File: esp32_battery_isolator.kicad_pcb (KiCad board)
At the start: 4 copper layers, 67.8 x 65.8 mm, 88 parts, among them J1 BATT1, J2 Conn_01x04_Female, J3 USB_B_Micro, J4 BATT2, J5 LOAD1, J6 CHGR, J7 LOAD2, J8 LOAD3, J9 Conn_01x03_Male, Q1 MMBT3904, Q10 AONR21321, Q11 AONR21321, Q12 MMBT3904, Q13 AONR21321, Q2 AONR21321, Q3 MMBT3904, Q4 AONR21321, Q5 MMBT3904, Q6 AONR21321, Q7 MMBT3904, Q8 AONR21321, Q9 MMBT3904, SW1 C492887, SW2 C492887, U1 ESP32-WROOM-32D, U2 XL1509_SOP8, U3 ADC128D818, U4 CC6903SO-30A, U5 CH340N, U6 CC6903SO-30A

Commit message: closer
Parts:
- removed Q13, Q6: AONR21321, Acea:DFN-TRANS_AONR21321
- removed Q5: MMBT3904, Package_TO_SOT_SMD:SOT-23
- removed R15: 200k, Resistor_SMD:R_0603_1608Metric
- removed R25: 11k, Resistor_SMD:R_0603_1608Metric
- removed R29: 510R, Resistor_SMD:R_0603_1608Metric
- added BZ1: Buzzer, Buzzer_Beeper:SMDBuzzer_C201046, F.Cu at (171.9, 122.0)
- Q10, Q11, Q2, Q4, Q8: value AONR21321 -> AONR21357
- moved U4 2.90 mm to (128.1, 96.8)
- moved U6 2.25 mm to (123.9, 104.7)
- moved Q4 1.38 mm to (122.2, 88.0)
- moved Ref** 1.34 mm to (111.5, 122.8)
- moved J2 1.13 mm to (158.0, 90.6)
- moved Q11 0.92 mm to (122.2, 92.2)
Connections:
- J9 pad 1: B2C -> COM
- Q10 pad S: B2C -> COM
- Q2 pad S: B2C -> COM
- Q8 pad S: B2C -> COM
- R14 pad 1: B1VM -> COM
- R16 pad 1: B2VM -> COM
- R17 pad 1: B2VM -> COM
- R20 pad 1: B2VM -> COM
- U1 pad 10: B2ON -> (no net)
- U1 pad 30: (no net) -> BZR
- U5 pad 4: (no net) -> RST
- U6 pad 3: B2C -> COM
- U6 pad 4: B2C -> COM
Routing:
- net BZR: track 0.00 -> 52.8 mm, vias 0 -> 4
- net COM: track 0.00 -> 37.4 mm, vias 3 -> 38
- net RST: track 46.1 -> 74.1 mm, vias 0 -> 2
- net Net-(Q13-PadG): track 22.5 -> 0.00 mm
- net B2VM: track 224.4 -> 209.4 mm, vias 14 -> 12
- net B2ON: track 13.1 -> 0.00 mm
- net Net-(Q5-Pad1): track 3.46 -> 0.00 mm
- net B1CM: track 46.1 -> 49.0 mm
- net L1ON: track 23.4 -> 25.9 mm
- net +3V3: track 138.2 -> 136.5 mm
- net B2C: track 1.60 -> 0.00 mm, vias 66 -> 0
- net Net-(Q1-Pad3): track 13.9 -> 14.9 mm
- net GND: track 72.5 -> 71.6 mm
- net L2ON: track 23.8 -> 24.4 mm
- net SCL: track 31.6 -> 31.1 mm
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- added copper zone on In2.Cu, net COM
- removed copper zone on B.Cu, net B2C
- removed copper zone on F.Cu, net B2C
- removed copper zone on In2.Cu, net B2C
- removed copper zone on B.Cu, net Net-(Q13-PadD)
- removed copper zone on F.Cu, net Net-(Q13-PadD)
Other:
- board text added: "ALARM"
- board text added: "CHGR"
- board text added: "ISOLATOR V1"
- board text removed: "B3/ CHG"

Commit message: closer
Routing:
- net L2ON: track 24.4 -> 26.3 mm
- net COM: vias 38 -> 39

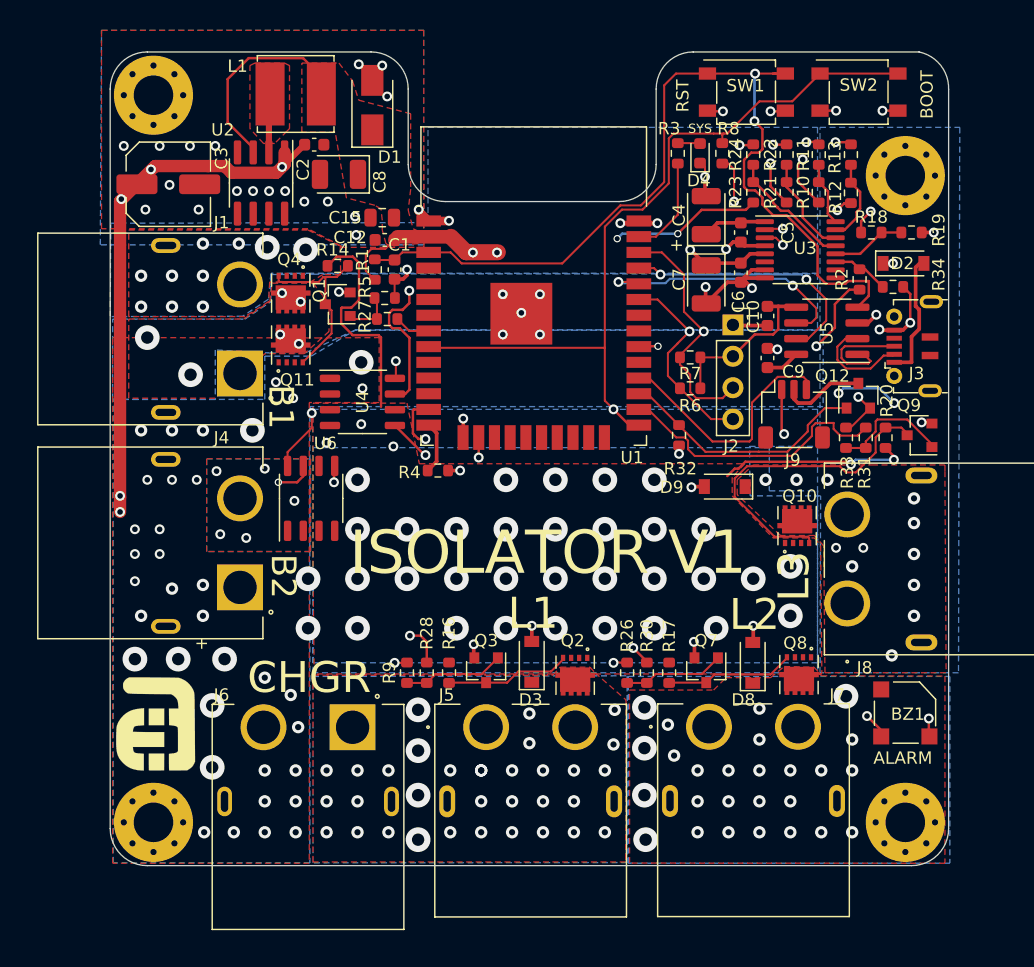
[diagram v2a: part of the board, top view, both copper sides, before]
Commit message: fixed daily couters not resetting
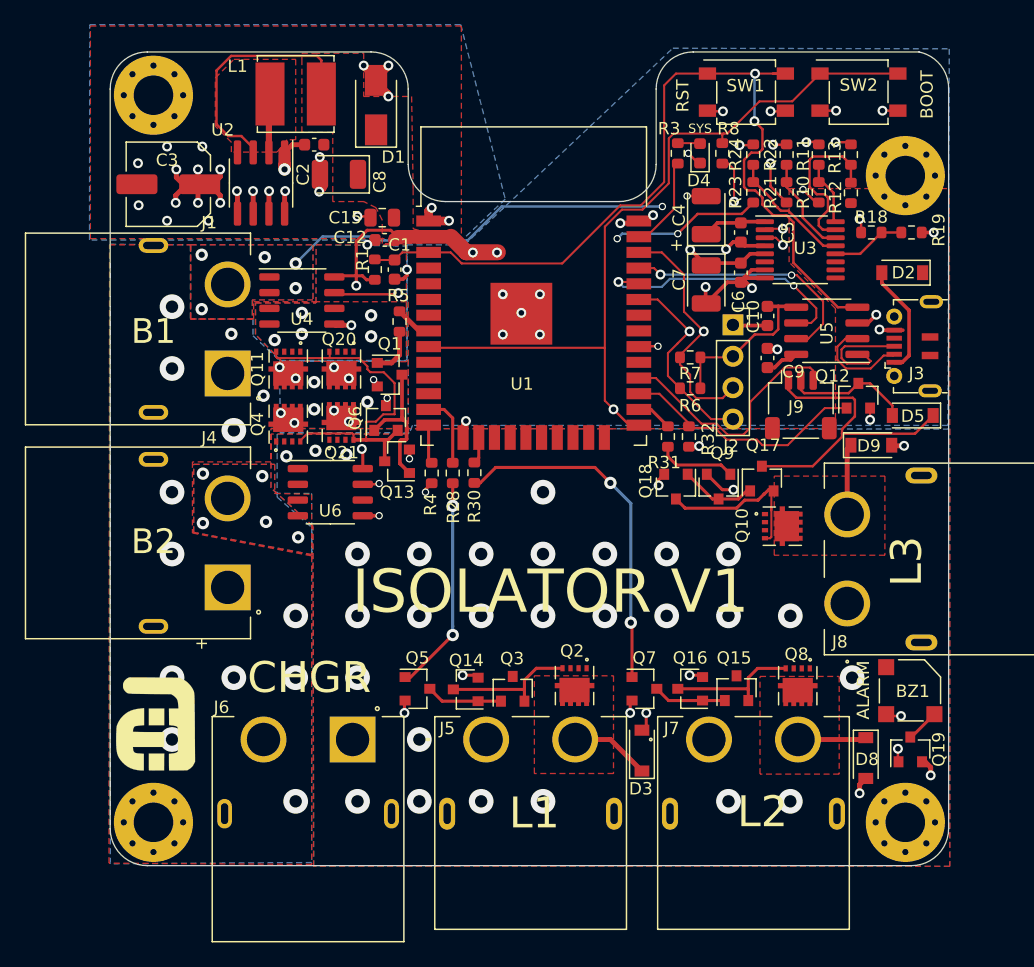
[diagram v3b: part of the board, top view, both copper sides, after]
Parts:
- removed R14, R16, R17, R2, R20: 200k, Resistor_SMD:R_0603_1608Metric
- removed R26, R33, R9: 11k, Resistor_SMD:R_0603_1608Metric
- removed R27: 510R, Resistor_SMD:R_0603_1608Metric
- removed R34: 33k, Resistor_SMD:R_0603_1608Metric
- added D5: B5819W, Diode_SMD:D_SOD-123, F.Cu at (172.6, 98.0)
- added Q13: MMBT3906, Package_TO_SOT_SMD:SOT-23, F.Cu at (130.8, 101.7)
- added Q14: MMBT3906, Package_TO_SOT_SMD:SOT-23, F.Cu at (136.4, 120.1)
- added Q15: MMBT3904, Package_TO_SOT_SMD:SOT-23, F.Cu at (158.3, 120.0)
- added Q16: MMBT3906, Package_TO_SOT_SMD:SOT-23, F.Cu at (154.6, 120.0)
- added Q17: MMBT3904, Package_TO_SOT_SMD:SOT-23, F.Cu at (160.3, 103.0)
- added Q18: MMBT3906, Package_TO_SOT_SMD:SOT-23, F.Cu at (153.4, 103.7)
- added Q19: MMBT3904, Package_TO_SOT_SMD:SOT-23, F.Cu at (172.3, 125.0)
- added Q20: AONR21357, Acea:DFN-TRANS_AONR21321, F.Cu at (126.3, 94.2)
- added Q21: AONR21357, Acea:DFN-TRANS_AONR21321, F.Cu at (126.3, 98.5)
- added Q5: MMBT3904, Package_TO_SOT_SMD:SOT-23, F.Cu at (132.5, 120.0)
- added Q6: MMBT3904, Package_TO_SOT_SMD:SOT-23, F.Cu at (129.9, 98.2)
- R5: value 11k -> 510R
- SW1, SW2: value C492887 -> C480325
- moved R30 21.4 mm to (137.1, 102.6)
- moved Q9 16.8 mm to (156.8, 103.7), turned to 270 degrees
- moved R28 16.3 mm to (135.3, 102.6)
- moved R31 16.0 mm to (152.8, 99.7)
- moved D9 12.3 mm to (169.2, 100.3), turned to 0 degrees
- moved D8 12.0 mm to (168.8, 125.7), turned to 270 degrees
- moved D3 11.4 mm to (150.7, 125.0)
- moved Q4 10.6 mm to (122.0, 98.7), turned to 90 degrees
- moved U4 9.55 mm to (123.2, 88.7)
- moved Q1 7.08 mm to (130.2, 94.7), turned to 0 degrees
- moved Q7 5.22 mm to (150.8, 120.0), turned to 0 degrees
- moved Q3 2.62 mm to (140.2, 120.0), turned to 90 degrees
- moved R5 2.25 mm to (131.1, 90.3), turned to 270 degrees
- moved Q11 1.95 mm to (122.0, 94.2), turned to 270 degrees
- moved BZ1 1.84 mm to (172.3, 120.2)
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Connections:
- net Net-(Q11-PadD) renamed D
- BZ1 pad 1: GND -> Net-(BZ1-Pad1)
- BZ1 pad 2: BZR -> +3V3
- C2 pad 1: B2VM -> COM
- C3 pad 1: B2VM -> COM
- D2 pad 1: B2VM -> COM
- J4 pad 2: B2VM -> Net-(J4-Pad2)
- Q11 pad G: Net-(Q1-Pad3) -> G
- Q2 pad G: Net-(Q2-PadG) -> Net-(Q14-Pad3)
- Q3 pad 1: Net-(Q3-Pad1) -> Net-(Q14-Pad1)
- Q3 pad 2: GND -> Net-(Q14-Pad3)
- Q3 pad 3: Net-(Q2-PadG) -> COM
- Q4 pad G: Net-(Q1-Pad3) -> G
- Q4 pad S: B1VM -> COM
- Q7 pad 3: Net-(Q7-Pad3) -> Net-(Q15-Pad1)
- Q8 pad G: Net-(Q7-Pad3) -> Net-(Q15-Pad2)
- Q9 pad 3: Net-(Q10-PadG) -> Net-(Q17-Pad1)
- R12 pad 1: B2VM -> COM
- R28 pad 2: Net-(Q3-Pad1) -> Net-(Q5-Pad1)
- R5 pad 1: Net-(Q1-Pad1) -> B1ON
- R5 pad 2: GND -> Net-(Q1-Pad1)
- U2 pad 1: B2VM -> COM
- U3 pad 11: B1CD -> (no net)
- U4 pad 1: B1C -> B1VM
- U4 pad 2: B1C -> B1VM
- U4 pad 3: COM -> B1C
- U4 pad 4: COM -> B1C
- U6 pad 1: B2VM -> COM
- U6 pad 2: B2VM -> COM
- U6 pad 3: COM -> Net-(J4-Pad2)
- U6 pad 4: COM -> Net-(J4-Pad2)
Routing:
- net B2VM: track 209.4 -> 0.00 mm, vias 12 -> 0
- net COM: track 37.4 -> 85.3 mm, vias 39 -> 36
- net +3V3: track 136.5 -> 169.8 mm, vias 7 -> 8
- net G: track 0.00 -> 29.4 mm
- net L2ON: track 26.3 -> 2.17 mm, vias 2 -> 0
- net Net-(Q7-Pad1): track 8.19 -> 28.5 mm, vias 0 -> 2
- net L1ON: track 25.9 -> 5.85 mm, vias 2 -> 0
- net L3ON: track 22.8 -> 2.92 mm
- net Net-(Q5-Pad1): track 0.00 -> 17.5 mm, vias 0 -> 2
- net Net-(Q10-PadG): track 26.5 -> 13.4 mm
- net Net-(Q14-Pad3): track 0.00 -> 11.0 mm
- net Net-(Q15-Pad2): track 0.00 -> 10.9 mm
- net Net-(Q7-Pad3): track 10.4 -> 0.00 mm
- net Net-(Q2-PadG): track 10.1 -> 0.00 mm
- net GND: track 71.6 -> 81.4 mm, vias 61 -> 62
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- added copper zone on In2.Cu, net B1C
- added copper zone on In2.Cu, net B1VM
- added copper zone on B.Cu, net Net-(J4-Pad2)
- added copper zone on F.Cu, net Net-(J4-Pad2)
- removed copper zone on B.Cu, net B2VM
- removed copper zone on F.Cu, net B2VM
- removed copper zone on In2.Cu, net COM
- removed copper zone on B.Cu, net LOAD1
- removed copper zone on B.Cu, net LOAD2
- removed copper zone on B.Cu, net LOAD3

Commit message: wip
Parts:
- removed D8, D9: B5819W, Diode_SMD:D_SOD-123
- removed the H1 at (111.2, 130.8)
- removed the H1 at (171.9, 78.5)
- removed the H1 at (171.9, 130.8)
- removed the H1 at (111.2, 72.0)
- removed J3: USB_B_Micro, Acea:USB_Micro_SHOU-HAN-MicroXNJ_C404969_Horizontal
- removed J4: BATT2, Acea:AMASS_XT60PW-M
- removed J5: LOAD1, Acea:AMASS_XT60PW-F
- removed J6: CHGR, Acea:AMASS_XT60PW-M
- removed J7: LOAD2, Acea:AMASS_XT60PW-F
- removed J8: LOAD3, Acea:AMASS_XT60PW-F
- removed J9: Conn_01x03_Male, Connector_JST:JST_SH_SM03B-SRSS-TB_1x03-1MP_P1.00mm_Horizontal
- removed R13: 33k, Resistor_SMD:R_0603_1608Metric
- removed R24, R32: 11k, Resistor_SMD:R_0603_1608Metric
- removed R30, R31: 510R, Resistor_SMD:R_0603_1608Metric
- removed Ref**: Val**, Acea:aces_electronics_small
- added C11: 100n, Capacitor_SMD:C_0603_1608Metric, F.Cu at (110.7, 112.7)
- added C13: 1uF, Capacitor_Tantalum_SMD:CP_EIA-3528-21_Kemet-B, F.Cu at (118.2, 66.5)
- added C14: 100n, Capacitor_SMD:C_0603_1608Metric, F.Cu at (121.8, 66.3)
- added C16: 1uF, Capacitor_Tantalum_SMD:CP_EIA-3528-21_Kemet-B, F.Cu at (118.2, 70.0)
- added C17: 100n, Capacitor_SMD:C_0603_1608Metric, F.Cu at (192.8, 106.5)
- added C18: 100n, Capacitor_SMD:C_0603_1608Metric, F.Cu at (149.4, 110.8)
- added D6: B5819W, Diode_SMD:D_SOD-123, F.Cu at (178.8, 129.9)
- added D7: B5819W, Diode_SMD:D_SOD-123, F.Cu at (161.8, 129.9)
- added H1: Cable_Connection, Acea:Rivneut_M6_Via, F.Cu at (117.7, 54.1)
- added H10: Cable_Connection, Acea:Rivneut_M6_Via, F.Cu at (152.7, 124.2)
- added H11: MountingHole, MountingHole:MountingHole_3.2mm_M3_Pad_Via, F.Cu at (135.7, 129.9)
- added H12: MountingHole, MountingHole:MountingHole_3.2mm_M3_Pad_Via, F.Cu at (112.0, 69.8)
- added H2: Cable_Connection, Acea:Rivneut_M6_Via, F.Cu at (117.7, 84.7)
- added H3: Cable_Connection, Acea:Rivneut_M6_Via, F.Cu at (135.7, 106.0)
- added H4: Cable_Connection, Acea:Rivneut_M6_Via, F.Cu at (169.7, 106.2)
- added H5: Cable_Connection, Acea:Rivneut_M6_Via, F.Cu at (117.7, 124.2)
- added H7: MountingHole, MountingHole:MountingHole_3.2mm_M3_Pad_Via, F.Cu at (169.7, 130.1)
- added H8: MountingHole, MountingHole:MountingHole_3.2mm_M3_Pad_Via, F.Cu at (194.2, 55.1)
- added H9: Cable_Connection, Acea:Rivneut_M6_Via, F.Cu at (187.7, 124.2)
- added R14: 11k, Resistor_SMD:R_0603_1608Metric, F.Cu at (169.6, 78.0)
- added R15: 510R, Resistor_SMD:R_0603_1608Metric, F.Cu at (165.9, 68.0)
- added R16: 4mR, Acea:RS1050Metric_Pad5.3x2.5mm, F.Cu at (116.3, 109.0)
- added R2: 3.6k, Resistor_SMD:R_0603_1608Metric, F.Cu at (189.4, 54.1)
- added R20: 510R, Resistor_SMD:R_0603_1608Metric, F.Cu at (187.1, 72.2)
- added R26: 200k, Resistor_SMD:R_0603_1608Metric, F.Cu at (131.7, 66.7)
- added R27: 33k, Resistor_SMD:R_0603_1608Metric, F.Cu at (133.2, 66.7)
- added R29: 33k, Resistor_SMD:R_0603_1608Metric, F.Cu at (133.2, 70.0)
- added R9: 4mR, Acea:RS1050Metric_Pad5.3x2.5mm, F.Cu at (130.2, 81.3)
- added U10: INA219BxDCN, Package_TO_SOT_SMD:SOT-23-8, F.Cu at (149.3, 108.2)
- added U7: INA219BxDCN, Package_TO_SOT_SMD:SOT-23-8, F.Cu at (110.7, 110.0)
- added U8: ADC128D818, Package_SO:TSSOP-16_4.4x5mm_P0.65mm, F.Cu at (126.5, 68.5)
- added U9: INA219BxDCN, Package_TO_SOT_SMD:SOT-23-8, F.Cu at (192.7, 109.0)
- BZ1: footprint Buzzer_Beeper:SMDBuzzer_C201046 -> Acea:SMDBuzzer_C201046
- C1: value 100n -> 4.7uF; footprint Capacitor_SMD:C_0603_1608Metric -> Capacitor_SMD:C_0805_2012Metric
- C15: value 4.7uF -> 100n; footprint Capacitor_SMD:C_0805_2012Metric -> Capacitor_SMD:C_0603_1608Metric
- C2: value 1uF -> 100n
- C3: value 220uF -> 100n; footprint Capacitor_SMD:C_Elec_6.3x7.7 -> Capacitor_SMD:C_0603_1608Metric
- C4: value 1uF -> 100n; footprint Capacitor_Tantalum_SMD:CP_EIA-3528-21_Kemet-B -> Capacitor_SMD:C_0603_1608Metric
- C7: footprint Capacitor_Tantalum_SMD:CP_EIA-3528-21_Kemet-B -> Capacitor_SMD:C_0603_1608Metric
- C8: footprint Capacitor_Tantalum_SMD:CP_EIA-3528-15_AVX-H -> Capacitor_SMD:C_Elec_6.3x7.7
- C9: value 100n -> 220uF; footprint Capacitor_SMD:C_0603_1608Metric -> Capacitor_Tantalum_SMD:CP_EIA-3528-15_AVX-H
- D1: value SS34 -> LED_Small; footprint Diode_SMD:D_SMA -> LED_SMD:LED_0603_1608Metric
- D4: value LED_Small -> SS34; footprint LED_SMD:LED_0603_1608Metric -> Diode_SMD:D_SMA
- J1: value BATT1 -> Conn_01x03_Male; footprint Acea:AMASS_XT60PW-M -> Connector_JST:JST_SH_SM03B-SRSS-TB_1x03-1MP_P1.00mm_Horizontal
- J2: value Conn_01x04_Female -> USB_C_Receptacle_USB2.0; footprint Connector_PinSocket_2.54mm:PinSocket_1x04_P2.54mm_Vertical -> Connector_USB:USB_C_Receptacle_HRO_TYPE-C-31-M-12
- Q10, Q2, Q8: value AONR21357 -> MMBT3904; footprint Acea:DFN-TRANS_AONR21321 -> Package_TO_SOT_SMD:SOT-23
- Q11, Q20: value AONR21357 -> MMBT3906; footprint Acea:DFN-TRANS_AONR21321 -> Package_TO_SOT_SMD:SOT-23
- Q12: value MMBT3904 -> AONR21357; footprint Package_TO_SOT_SMD:SOT-23 -> Acea:DFN-TRANS_AONR21321
- Q13, Q14: value MMBT3906 -> MMBT3904
- Q18: value MMBT3906 -> AONR21357; footprint Package_TO_SOT_SMD:SOT-23 -> Acea:DFN-TRANS_AONR21321
- Q3: value MMBT3904 -> MMBT3906
- Q4: value AONR21357 -> HSBA100P03; footprint Acea:DFN-TRANS_AONR21321 -> Acea:LFPAK56
- Q5, Q6, Q7: value MMBT3904 -> HSBA100P03; footprint Package_TO_SOT_SMD:SOT-23 -> Acea:LFPAK56
- R1: value 11k -> 510R
- R10, R12: value 200k -> 4mR; footprint Resistor_SMD:R_0603_1608Metric -> Acea:RS1050Metric_Pad5.3x2.5mm
- R11: value 33k -> 3.6k
- R18: value 3.6k -> 5.1k; footprint Resistor_SMD:R_0603_1608Metric -> Resistor_SMD:R_0402_1005Metric
- R19: value 11k -> 5.1k; footprint Resistor_SMD:R_0603_1608Metric -> Resistor_SMD:R_0402_1005Metric
- R21: value 3.6k -> 510R
- R22, R4: value 11k -> 4mR; footprint Resistor_SMD:R_0603_1608Metric -> Acea:RS1050Metric_Pad5.3x2.5mm
- R23: value 3.6k -> 4mR; footprint Resistor_SMD:R_0603_1608Metric -> Acea:RS1050Metric_Pad5.3x2.5mm
- R28: value 510R -> 200k
- R3, R6, R7: value 3.6k -> 11k
- R5: value 510R -> 4mR; footprint Resistor_SMD:R_0603_1608Metric -> Acea:RS1050Metric_Pad5.3x2.5mm
- R8: value 11k -> 3.6k
- U2: value XL1509_SOP8 -> INA219BxDCN; footprint Package_SO:SOIC-8_3.9x4.9mm_P1.27mm -> Package_TO_SOT_SMD:SOT-23-8
- U3: value ADC128D818 -> INA219BxDCN; footprint Package_SO:TSSOP-16_4.4x5mm_P0.65mm -> Package_TO_SOT_SMD:SOT-23-8
- U4: value CC6903SO-30A -> INA219BxDCN; footprint Package_SO:SOP-8_3.9x4.9mm_P1.27mm -> Package_TO_SOT_SMD:SOT-23-8
- U5: value CH340N -> XL1509_SOP8
- U6: value CC6903SO-30A -> CH340N; footprint Package_SO:SOP-8_3.9x4.9mm_P1.27mm -> Package_SO:SOIC-8_3.9x4.9mm_P1.27mm
- moved U6 71.2 mm to (192.7, 80.5), turned to 90 degrees
- moved C12 66.7 mm to (196.3, 78.8), turned to -90 degrees
- moved D1 63.8 mm to (189.7, 52.6), turned to 0 degrees
- moved Q13 58.3 mm to (183.1, 75.8), turned to -90 degrees
- moved C3 57.3 mm to (165.9, 59.0)
- moved R11 55.4 mm to (111.0, 64.0), turned to -90 degrees
- moved J1 55.0 mm to (164.8, 79.0), turned to 0 degrees
- moved Q3 54.1 mm to (159.1, 69.3), turned to -90 degrees
- moved U3 53.9 mm to (110.2, 76.2)
- moved Q10 52.8 mm to (109.8, 98.3), turned to 90 degrees
- moved Q2 51.3 mm to (154.6, 69.3)
- moved Q12 50.8 mm to (117.3, 98.5), turned to -90 degrees
- moved R8 49.5 mm to (109.3, 64.0), turned to -90 degrees
- moved C5 48.8 mm to (110.0, 79.0), turned to 0 degrees
- moved C2 48.6 mm to (167.2, 53.5), turned to 90 degrees
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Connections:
- C1 pad 1: RST -> +3V3
- C10 pad 1: +3V3 -> Net-(C10-Pad1)
- C2 pad 1: COM -> +3V3
- C3 pad 1: COM -> RST
- C4 pad 1: Net-(C4-Pad1) -> +3V3
- C5 pad 1: Net-(C4-Pad1) -> +3V3
- C7 pad 1: +3V3 -> COM
- C8 pad 1: +3V3 -> COM
- C9 pad 1: Net-(C9-Pad1) -> +3V3
- D1 pad 1: +3V3 -> GND
- D1 pad 2: GND -> Net-(D1-Pad2)
- D2 pad 2: 5V -> FANGND
- D4 pad 1: GND -> +3V3
- D4 pad 2: Net-(D4-Pad2) -> GND
- D5 pad 2: FANGND -> 5V
- J1 pad 1: GND -> COM
- J1 pad 2: B1VM -> FANGND
- Q12 pad 1: FANON -> Net-(Q10-Pad2)
- Q12 pad 2: GND -> Net-(Q12-Pad2)
- Q12 pad 3: FANGND -> COM
- Q13 pad 1: Net-(Q1-Pad3) -> BZR
- Q13 pad 3: G -> Net-(BZ1-Pad1)
- Q15 pad 1: Net-(Q15-Pad1) -> Net-(Q14-Pad3)
- Q16 pad 1: Net-(Q15-Pad1) -> Net-(Q14-Pad3)
- Q17 pad 2: Net-(Q10-PadG) -> GND
- Q17 pad 3: COM -> Net-(Q17-Pad3)
- Q18 pad 1: Net-(Q17-Pad1) -> Net-(Q15-Pad2)
- Q18 pad 2: GND -> Net-(Q18-Pad2)
- Q18 pad 3: Net-(Q10-PadG) -> COM
- Q19 pad 1: BZR -> Net-(Q17-Pad3)
- Q19 pad 2: GND -> Net-(Q19-Pad2)
- Q19 pad 3: Net-(BZ1-Pad1) -> COM
- Q3 pad 1: Net-(Q14-Pad1) -> Net-(Q1-Pad3)
- Q3 pad 2: Net-(Q14-Pad3) -> GND
- Q3 pad 3: COM -> G
- Q5 pad 1: Net-(Q5-Pad1) -> G
- Q5 pad 2: GND -> D
- Q5 pad 3: Net-(Q14-Pad1) -> COM
- Q6 pad 1: Net-(Q1-Pad3) -> G
- Q6 pad 2: G -> D
- Q6 pad 3: COM -> Net-(Q4-Pad3)
- Q7 pad 1: Net-(Q7-Pad1) -> G
- Q7 pad 2: GND -> D
- Q7 pad 3: Net-(Q15-Pad1) -> COM
- Q9 pad 3: Net-(Q17-Pad1) -> Net-(Q10-Pad1)
- R1 pad 1: +3V3 -> B1ON
- R1 pad 2: RST -> Net-(Q1-Pad1)
- R10 pad 1: B1VM -> Net-(H3-Pad1)
- R10 pad 2: B1VD -> COM
- R11 pad 1: B1VD -> +3V3
- R11 pad 2: GND -> SDA
- R12 pad 2: B2VD -> B2VM
- R18 pad 1: +3V3 -> GND
- R18 pad 2: 3v3VD -> Net-(J2-PadA5)
- R19 pad 1: 3v3VD -> GND
- R19 pad 2: GND -> Net-(J2-PadB5)
- R21 pad 1: B1CM -> L2ON
- R21 pad 2: B1CVD -> Net-(Q17-Pad1)
- R22 pad 1: B1CVD -> Net-(Q18-Pad2)
- R22 pad 2: GND -> LOAD3
- R23 pad 1: B2CM -> Net-(Q21-Pad2)
- R23 pad 2: B2CVD -> LOAD2
- R28 pad 1: L1ON -> COM
- R28 pad 2: Net-(Q5-Pad1) -> B2VD
- R3 pad 1: SYS_LED -> +3V3
- R3 pad 2: Net-(D4-Pad2) -> RST
- R4 pad 1: GND -> Net-(Q4-Pad3)
- R4 pad 2: Net-(R4-Pad2) -> B1VM
- R5 pad 1: B1ON -> Net-(Q4-Pad3)
- R5 pad 2: Net-(Q1-Pad1) -> B1VM
- R6 pad 2: SCL -> BOOT
- R7 pad 1: +3V3 -> GND
- R7 pad 2: SDA -> Net-(R7-Pad2)
- R8 pad 2: BOOT -> SCL
- U1 pad 10: (no net) -> unconnected-(U1-Pad10)
- U1 pad 11: (no net) -> unconnected-(U1-Pad11)
- U1 pad 12: (no net) -> unconnected-(U1-Pad12)
- U1 pad 14: Net-(R4-Pad2) -> Net-(R7-Pad2)
- U1 pad 17: (no net) -> unconnected-(U1-Pad17)
- U1 pad 18: (no net) -> unconnected-(U1-Pad18)
- U1 pad 19: (no net) -> unconnected-(U1-Pad19)
- U1 pad 20: (no net) -> unconnected-(U1-Pad20)
- U1 pad 21: (no net) -> unconnected-(U1-Pad21)
- U1 pad 22: (no net) -> unconnected-(U1-Pad22)
- U1 pad 23: (no net) -> unconnected-(U1-Pad23)
- U1 pad 24: (no net) -> unconnected-(U1-Pad24)
- U1 pad 29: (no net) -> unconnected-(U1-Pad29)
- U1 pad 31: (no net) -> unconnected-(U1-Pad31)
- U1 pad 32: (no net) -> unconnected-(U1-Pad32)
- U1 pad 4: (no net) -> unconnected-(U1-Pad4)
- U1 pad 5: (no net) -> unconnected-(U1-Pad5)
- U1 pad 6: (no net) -> unconnected-(U1-Pad6)
- U1 pad 7: (no net) -> unconnected-(U1-Pad7)
- U2 pad 1: COM -> B1VM
- U2 pad 2: Net-(L1-Pad1) -> Net-(Q4-Pad3)
- U2 pad 3: +3V3 -> GND
- U2 pad 4: (no net) -> +3V3
- U2 pad 5: GND -> SCL
- U2 pad 6: GND -> SDA
- U3 pad 1: Net-(C4-Pad1) -> B2VM
- U3 pad 2: SDA -> COM
- U3 pad 3: SCL -> GND
- U3 pad 4: GND -> +3V3
- U3 pad 5: +3V3 -> SCL
- U3 pad 6: (no net) -> SDA
- U3 pad 7: GND -> +3V3
- U4 pad 1: B1VM -> COM
- U4 pad 2: B1VM -> Net-(H3-Pad1)
- U4 pad 3: B1C -> GND
- U4 pad 4: B1C -> +3V3
- U4 pad 5: GND -> SCL
- U4 pad 6: (no net) -> SDA
- U4 pad 7: B1CM -> SDA
- U4 pad 8: +3V3 -> GND
- U5 pad 1: D+ -> COM
- U5 pad 2: D- -> Net-(L1-Pad1)
- U5 pad 3: GND -> +3V3
- U5 pad 4: RST -> unconnected-(U5-Pad4)
- U5 pad 5: +3V3 -> GND
- U5 pad 6: RXD -> GND
- U5 pad 7: TXD -> GND
- U5 pad 8: Net-(C9-Pad1) -> GND
- U6 pad 1: COM -> D+
- U6 pad 2: COM -> D-
- U6 pad 3: Net-(J4-Pad2) -> GND
- U6 pad 4: Net-(J4-Pad2) -> RST
- U6 pad 5: GND -> +3V3
- U6 pad 6: (no net) -> RXD
- U6 pad 7: B2CM -> TXD
- U6 pad 8: +3V3 -> Net-(C10-Pad1)
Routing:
- net +3V3: track 169.8 -> 0.00 mm, vias 8 -> 0
- net COM: track 85.3 -> 0.00 mm, vias 36 -> 0
- net GND: track 81.4 -> 0.00 mm, vias 62 -> 0
- net RST: track 72.0 -> 0.00 mm, vias 2 -> 0
- net BOOT: track 63.7 -> 0.00 mm, vias 1 -> 0
- net BZR: track 51.1 -> 0.00 mm, vias 2 -> 0
- net B2CM: track 48.2 -> 0.00 mm, vias 3 -> 0
- net B1VM: track 45.7 -> 0.00 mm, vias 7 -> 0
- net B1CM: track 43.4 -> 0.00 mm, vias 2 -> 0
- net SCL: track 31.1 -> 0.00 mm, vias 2 -> 0
- net G: track 29.4 -> 0.00 mm
- net SDA: track 29.1 -> 0.00 mm, vias 2 -> 0
- net Net-(Q7-Pad1): track 28.5 -> 0.00 mm, vias 2 -> 0
- net RXD: track 21.7 -> 0.00 mm, vias 2 -> 0
- net TXD: track 20.5 -> 0.00 mm, vias 2 -> 0
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- added copper zone on In2.Cu, net +3V3
- removed copper zone on F.Cu, net +3V3
- removed copper zone on B.Cu, net B1C
- removed copper zone on F.Cu, net B1C
- removed copper zone on In2.Cu, net B1C
- removed copper zone on B.Cu, net B1VM
- removed copper zone on F.Cu, net B1VM
- removed copper zone on In2.Cu, net B1VM
- removed copper zone on B.Cu, net COM
- removed copper zone on F.Cu, net COM
- removed copper zone on B.Cu, net D
- removed copper zone on F.Cu, net D
- removed copper zone on B.Cu, net GND
- removed copper zone on F.Cu, net GND
- removed copper zone on F.Cu, net LOAD1
- removed copper zone on F.Cu, net LOAD2
- removed copper zone on F.Cu, net LOAD3
- removed copper zone on B.Cu, net Net-(J4-Pad2)
- removed copper zone on F.Cu, net Net-(J4-Pad2)
- removed copper zone on F.Cu, net Net-(L1-Pad1)
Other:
- board size 67.8 x 65.8 mm -> 90 x 89.9 mm
- net class Default removed
- board text added: "BATT1"
- board text added: "BATT2"
- board text added: "GND"
- board text added: "LOAD1"
- board text added: "LOAD2"
- board text added: "LOAD3"
- board text removed: "+"

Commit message: 1st pass complete
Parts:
- C8: value 220uF -> 100uF(220uF); footprint Capacitor_SMD:C_Elec_6.3x7.7 -> Capacitor_SMD:C_Elec_6.3x5.4
- D3, D6, D7: footprint Diode_SMD:D_SOD-123 -> Diode_SMD:D_SMC
- J2: footprint Connector_USB:USB_C_Receptacle_HRO_TYPE-C-31-M-12 -> Acea:USB_C_Receptacle_HRO_TYPE-C-31-M-12
- R18, R19: footprint Resistor_SMD:R_0402_1005Metric -> Resistor_SMD:R_0603_1608Metric
- SW1, SW2: value C480325 -> C620183
- moved C17 28.4 mm to (169.7, 122.9), turned to 0 degrees
- moved U9 25.8 mm to (169.4, 120.2), turned to 0 degrees
- moved U7 21.7 mm to (129.8, 120.3)
- moved C11 21.5 mm to (129.6, 123.0)
- moved C18 15.1 mm to (140.3, 122.9)
- moved U10 15.0 mm to (140.2, 120.2), turned to 0 degrees
- moved C6 10.8 mm to (135.0, 123.0)
- moved U4 10.8 mm to (135.0, 120.3)
- moved Q15 9.10 mm to (179.7, 100.8), turned to 90 degrees
- moved R27 8.89 mm to (125.7, 71.3), turned to 180 degrees
- moved R26 8.65 mm to (125.7, 72.9), turned to 0 degrees
- moved R9 7.97 mm to (131.9, 89.2), turned to 135 degrees
- moved R20 6.55 mm to (187.1, 78.8), turned to -90 degrees
- moved Q20 5.70 mm to (146.7, 104.9), turned to -90 degrees
- moved Q14 4.80 mm to (179.7, 108.5), turned to -90 degrees
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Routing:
- net SDA: track 0.00 -> 254.5 mm, vias 0 -> 8
- net SCL: track 0.00 -> 252.9 mm, vias 0 -> 8
- net COM: track 0.00 -> 210.5 mm, vias 0 -> 21
- net Net-(Q9-Pad1): track 0.00 -> 143.1 mm, vias 0 -> 4
- net GND: track 0.00 -> 78.2 mm, vias 0 -> 80
- net RST: track 0.00 -> 60.5 mm, vias 0 -> 3
- net Net-(Q17-Pad1): track 0.00 -> 57.7 mm, vias 0 -> 2
- net G: track 0.00 -> 57.6 mm
- net +3V3: track 0.00 -> 56.5 mm, vias 0 -> 21
- net Net-(Q14-Pad1): track 0.00 -> 40.6 mm, vias 0 -> 2
- net BOOT: track 0.00 -> 37.1 mm, vias 0 -> 4
- net RXD: track 0.00 -> 30.5 mm
- net RPM: track 0.00 -> 29.5 mm
- net BZR: track 0.00 -> 28.7 mm
- net Net-(Q18-Pad2): track 0.00 -> 28.6 mm, vias 0 -> 3
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- added copper zone on F.Cu, net +3V3
- added copper zone on F.Cu, net B1VM
- added copper zone on F.Cu, net B2VM
- added copper zone on F.Cu, net COM
- added copper zone on B.Cu, net D
- added copper zone on F.Cu, net D
- added copper zone on F.Cu, net GND
- added copper zone on F.Cu, net LOAD1
- added copper zone on F.Cu, net LOAD2
- added copper zone on F.Cu, net LOAD3
- added copper zone on F.Cu, net Net-(H3-Pad1)
- added copper zone on F.Cu, net Net-(L1-Pad1)
- added copper zone on B.Cu, net Net-(Q12-Pad2)
- added copper zone on F.Cu, net Net-(Q12-Pad2)
- added copper zone on B.Cu, net Net-(Q18-Pad2)
- added copper zone on F.Cu, net Net-(Q18-Pad2)
- added copper zone on B.Cu, net Net-(Q21-Pad2)
- added copper zone on F.Cu, net Net-(Q21-Pad2)
- added copper zone on F.Cu, net Net-(Q4-Pad3)
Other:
- board text added: "ACEA QUIGG 12/21"
- board text added: "ISOLATOR R6"
- board text removed: "B1"
- board text removed: "B2"
- board text removed: "BATTERY ISOLATOR LITE REV. G ACEA QUIGG 09/21"
- board text removed: "ISOLATOR V1"
- board text removed: "L1"
- board text removed: "L2"
- board text removed: "L3"

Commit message: closer- ERC is good
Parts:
- added C8: 100uF(220uF), Capacitor_SMD:C_Elec_6.3x5.4, F.Cu at (140.9, 48.1)
- added Ref**: Val**, Acea:aces_electronics_small, F.Cu at (147.1, 89.2)
- moved R4 4.26 mm to (141.1, 58.6), turned to 100 degrees
- moved Q4 2.15 mm to (136.0, 67.6)
- moved Q6 0.90 mm to (147.8, 67.6)
- moved R5 0.50 mm to (132.2, 54.5), turned to 100 degrees
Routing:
- net GND: track 78.2 -> 87.5 mm, vias 80 -> 83
- net Net-(Q4-Pad3): track 10.4 -> 7.31 mm, vias 3 -> 4
- net COM: track 210.5 -> 213.4 mm
- net G: track 57.6 -> 60.4 mm
- net D: vias 32 -> 31
- net B1VM: vias 8 -> 7
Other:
- board text added: "====D"
